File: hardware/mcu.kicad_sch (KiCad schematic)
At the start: 56 parts, among them J10 PRPC001DAAN-RC, J11 PRPC006SAAN-RC, J12 PRPC004SAAN-RC, J8 SBH11-NBPC-D05-SM-BK, J9 PRPC006SAAN-RC, U5 AT25SF081B-SSHD-B, U6 MCP9808T-E/MS, U7 STM32L552CET6, Y1 ABS05-32.768KHZ-9-T, Y2 ECS-160-9-37-CKM-TR3

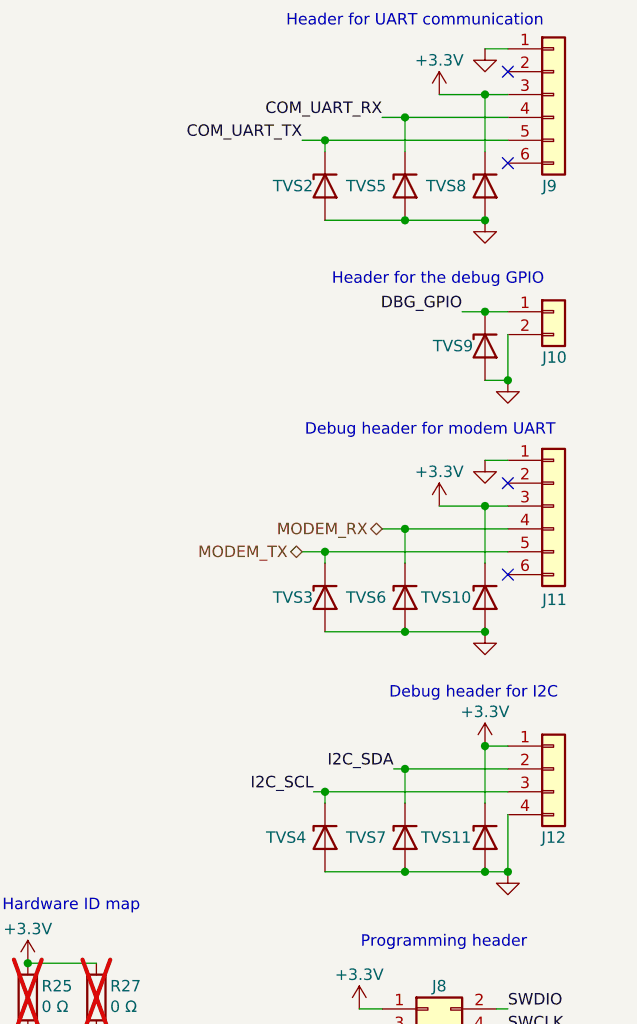
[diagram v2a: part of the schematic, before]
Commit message: HW: Re-layout TVS diodes
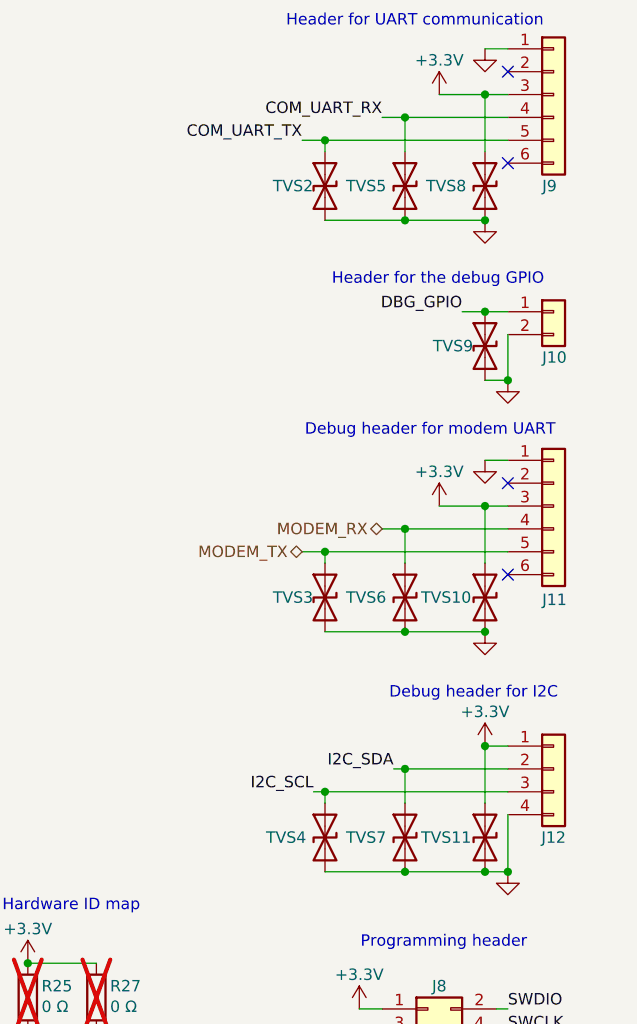
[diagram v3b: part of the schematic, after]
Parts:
- TVS10, TVS11, TVS2, TVS3, TVS4, TVS5, TVS6, TVS7, TVS8, TVS9: value CPDUC5V0USP-HF -> CPDQC5V0ESPC-HF; footprint Diode_SMD:D_0603_1608Metric_Pad1.05x0.95mm_HandSolder -> Diode_SMD:D_0402_1005Metric_Pad0.77x0.64mm_HandSolder; symbol Device:D_Zener -> Device:D_TVS; Digi-Key Part Number 641-1765-1-ND -> 641-1895-1-ND; Manufacturer Part Number CPDUC5V0USP-HF -> CPDQC5V0ESPC-HF
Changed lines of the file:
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@@
 	)
 	(symbol
-		(lib_id "Device:D_Zener")
+		(lib_id "Device:D_TVS")
 		(at 271.78 101.6 90)
 		(mirror x)
@@
 			)
 		)
-		(property "Value" "CPDUC5V0USP-HF"
+		(property "Value" "CPDQC5V0ESPC-HF"
 			(at 261.62 102.87 90)
 			(effects
@@
 			)
 		)
-		(property "Footprint" "Diode_SMD:D_0603_1608Metric_Pad1.05x0.95mm_HandSolder"
+		(property "Footprint" "Diode_SMD:D_0402_1005Metric_Pad0.77x0.64mm_HandSolder"
 			(at 271.78 101.6 0)
 			(effects
@@
 			)
 		)
-		(property "Description" ""
+		(property "Description" "Bidirectional transient-voltage-suppression diode"
 			(at 271.78 101.6 0)
 			(effects
@@
 			)
 		)
-		(property "Digi-Key Part Number" "641-1765-1-ND"
+		(property "Digi-Key Part Number" "641-1895-1-ND"
 			(at 271.78 101.6 0)
 			(effects
@@
 			)
 		)
-		(property "Manufacturer Part Number" "CPDUC5V0USP-HF"
+		(property "Manufacturer Part Number" "CPDQC5V0ESPC-HF"
 			(at 271.78 101.6 0)
 			(effects
@@
 	)
 	(symbol
-		(lib_id "Device:D_Zener")
+		(lib_id "Device:D_TVS")
 		(at 254 101.6 90)
 		(mirror x)
@@
 			)
 		)
-		(property "Value" "CPDUC5V0USP-HF"
+		(property "Value" "CPDQC5V0ESPC-HF"
 			(at 243.84 102.87 90)
 			(effects
@@
 			)
 		)
-		(property "Footprint" "Diode_SMD:D_0603_1608Metric_Pad1.05x0.95mm_HandSolder"
+		(property "Footprint" "Diode_SMD:D_0402_1005Metric_Pad0.77x0.64mm_HandSolder"
 			(at 254 101.6 0)
 			(effects
@@
 			)
 		)
-		(property "Description" ""
+		(property "Description" "Bidirectional transient-voltage-suppression diode"
 			(at 254 101.6 0)
 			(effects
@@
 			)
 		)
-		(property "Digi-Key Part Number" "641-1765-1-ND"
+		(property "Digi-Key Part Number" "641-1895-1-ND"
 			(at 254 101.6 0)
 			(effects
@@
 			)
 		)
-		(property "Manufacturer Part Number" "CPDUC5V0USP-HF"
+		(property "Manufacturer Part Number" "CPDQC5V0ESPC-HF"
 			(at 254 101.6 0)
 			(effects
@@
 	)
 	(symbol
-		(lib_id "Device:D_Zener")
+		(lib_id "Device:D_TVS")
 		(at 271.78 73.66 90)
 		(mirror x)
@@
 			)
 		)
-		(property "Value" "CPDUC5V0USP-HF"
+		(property "Value" "CPDQC5V0ESPC-HF"
 			(at 261.62 74.93 90)
 			(effects
@@
 			)
 		)
-		(property "Footprint" "Diode_SMD:D_0603_1608Metric_Pad1.05x0.95mm_HandSolder"
+		(property "Footprint" "Diode_SMD:D_0402_1005Metric_Pad0.77x0.64mm_HandSolder"
 			(at 271.78 73.66 0)
 			(effects
@@
 			)
 		)
-		(property "Description" ""
+		(property "Description" "Bidirectional transient-voltage-suppression diode"
 			(at 271.78 73.66 0)
 			(effects
@@
 			)
 		)
-		(property "Digi-Key Part Number" "641-1765-1-ND"
+		(property "Digi-Key Part Number" "641-1895-1-ND"
 			(at 271.78 73.66 0)
 			(effects
@@
 			)
 		)
-		(property "Manufacturer Part Number" "CPDUC5V0USP-HF"
+		(property "Manufacturer Part Number" "CPDQC5V0ESPC-HF"
 			(at 271.78 73.66 0)
 			(effects
@@
 	)
 	(symbol
-		(lib_id "Device:D_Zener")
+		(lib_id "Device:D_TVS")
 		(at 262.89 101.6 90)
 		(mirror x)
@@
 			)
 		)
-		(property "Value" "CPDUC5V0USP-HF"
+		(property "Value" "CPDQC5V0ESPC-HF"
 			(at 252.73 102.87 90)
 			(effects
@@
 			)
 		)
-		(property "Footprint" "Diode_SMD:D_0603_1608Metric_Pad1.05x0.95mm_HandSolder"
+		(property "Footprint" "Diode_SMD:D_0402_1005Metric_Pad0.77x0.64mm_HandSolder"
 			(at 262.89 101.6 0)
 			(effects
@@
 			)
 		)
-		(property "Description" ""
+		(property "Description" "Bidirectional transient-voltage-suppression diode"
 			(at 262.89 101.6 0)
 			(effects
@@
 			)
 		)
-		(property "Digi-Key Part Number" "641-1765-1-ND"
+		(property "Digi-Key Part Number" "641-1895-1-ND"
 			(at 262.89 101.6 0)
 			(effects
@@
 			)
 		)
-		(property "Manufacturer Part Number" "CPDUC5V0USP-HF"
+		(property "Manufacturer Part Number" "CPDQC5V0ESPC-HF"
 			(at 262.89 101.6 0)
 			(effects
@@
 	)
 	(symbol
-		(lib_id "Device:D_Zener")
+		(lib_id "Device:D_TVS")
 		(at 262.89 55.88 90)
 		(mirror x)
@@
 			)
 		)
-		(property "Value" "CPDUC5V0USP-HF"
+		(property "Value" "CPDQC5V0ESPC-HF"
 			(at 252.73 57.15 90)
 			(effects
@@
 			)
 		)
-		(property "Footprint" "Diode_SMD:D_0603_1608Metric_Pad1.05x0.95mm_HandSolder"
+		(property "Footprint" "Diode_SMD:D_0402_1005Metric_Pad0.77x0.64mm_HandSolder"
 			(at 262.89 55.88 0)
 			(effects
@@
 			)
 		)
-		(property "Description" ""
+		(property "Description" "Bidirectional transient-voltage-suppression diode"
 			(at 262.89 55.88 0)
 			(effects
@@
 			)
 		)
-		(property "Digi-Key Part Number" "641-1765-1-ND"
+		(property "Digi-Key Part Number" "641-1895-1-ND"
 			(at 262.89 55.88 0)
 			(effects
@@
 			)
 		)
-		(property "Manufacturer Part Number" "CPDUC5V0USP-HF"
+		(property "Manufacturer Part Number" "CPDQC5V0ESPC-HF"
 			(at 262.89 55.88 0)
 			(effects
@@
 	)
 	(symbol
-		(lib_id "Device:D_Zener")
+		(lib_id "Device:D_TVS")
 		(at 271.78 55.88 90)
 		(mirror x)
@@
 			)
 		)
-		(property "Value" "CPDUC5V0USP-HF"
+		(property "Value" "CPDQC5V0ESPC-HF"
 			(at 261.62 57.15 90)
 			(effects
@@
 			)
 		)
-		(property "Footprint" "Diode_SMD:D_0603_1608Metric_Pad1.05x0.95mm_HandSolder"
+		(property "Footprint" "Diode_SMD:D_0402_1005Metric_Pad0.77x0.64mm_HandSolder"
 			(at 271.78 55.88 0)
 			(effects
@@
 			)
 		)
-		(property "Description" ""
+		(property "Description" "Bidirectional transient-voltage-suppression diode"
 			(at 271.78 55.88 0)
 			(effects
@@
 			)
 		)
-		(property "Digi-Key Part Number" "641-1765-1-ND"
+		(property "Digi-Key Part Number" "641-1895-1-ND"
 			(at 271.78 55.88 0)
 			(effects
@@
 			)
 		)
-		(property "Manufacturer Part Number" "CPDUC5V0USP-HF"
+		(property "Manufacturer Part Number" "CPDQC5V0ESPC-HF"
 			(at 271.78 55.88 0)
 			(effects
@@
 	)
 	(symbol
-		(lib_id "Device:D_Zener")
+		(lib_id "Device:D_TVS")
 		(at 254 128.27 90)
 		(mirror x)
@@
 			)
 		)
-		(property "Value" "CPDUC5V0USP-HF"
+		(property "Value" "CPDQC5V0ESPC-HF"
 			(at 243.84 129.54 90)
 			(effects
@@
 			)
 		)
-		(property "Footprint" "Diode_SMD:D_0603_1608Metric_Pad1.05x0.95mm_HandSolder"
+		(property "Footprint" "Diode_SMD:D_0402_1005Metric_Pad0.77x0.64mm_HandSolder"
 			(at 254 128.27 0)
 			(effects
@@
 			)
 		)
-		(property "Description" ""
+		(property "Description" "Bidirectional transient-voltage-suppression diode"
 			(at 254 128.27 0)
 			(effects
@@
 			)
 		)
-		(property "Digi-Key Part Number" "641-1765-1-ND"
+		(property "Digi-Key Part Number" "641-1895-1-ND"
 			(at 254 128.27 0)
 			(effects
@@
 			)
 		)
-		(property "Manufacturer Part Number" "CPDUC5V0USP-HF"
+		(property "Manufacturer Part Number" "CPDQC5V0ESPC-HF"
 			(at 254 128.27 0)
 			(effects
@@
 	)
 	(symbol
-		(lib_id "Device:D_Zener")
+		(lib_id "Device:D_TVS")
 		(at 254 55.88 90)
 		(mirror x)
@@
 			)
 		)
-		(property "Value" "CPDUC5V0USP-HF"
+		(property "Value" "CPDQC5V0ESPC-HF"
 			(at 243.84 57.15 90)
 			(effects
@@
 			)
 		)
-		(property "Footprint" "Diode_SMD:D_0603_1608Metric_Pad1.05x0.95mm_HandSolder"
+		(property "Footprint" "Diode_SMD:D_0402_1005Metric_Pad0.77x0.64mm_HandSolder"
 			(at 254 55.88 0)
 			(effects
@@
 			)
 		)
-		(property "Description" ""
+		(property "Description" "Bidirectional transient-voltage-suppression diode"
 			(at 254 55.88 0)
 			(effects
@@
 			)
 		)
-		(property "Digi-Key Part Number" "641-1765-1-ND"
+		(property "Digi-Key Part Number" "641-1895-1-ND"
 			(at 254 55.88 0)
 			(effects
@@
 			)
 		)
-		(property "Manufacturer Part Number" "CPDUC5V0USP-HF"
+		(property "Manufacturer Part Number" "CPDQC5V0ESPC-HF"
 			(at 254 55.88 0)
 			(effects
@@
 	)
 	(symbol
-		(lib_id "Device:D_Zener")
+		(lib_id "Device:D_TVS")
 		(at 262.89 128.27 90)
 		(mirror x)
@@
 			)
 		)
-		(property "Value" "CPDUC5V0USP-HF"
+		(property "Value" "CPDQC5V0ESPC-HF"
 			(at 252.73 129.54 90)
 			(effects
@@
 			)
 		)
-		(property "Footprint" "Diode_SMD:D_0603_1608Metric_Pad1.05x0.95mm_HandSolder"
+		(property "Footprint" "Diode_SMD:D_0402_1005Metric_Pad0.77x0.64mm_HandSolder"
 			(at 262.89 128.27 0)
 			(effects
@@
 			)
 		)
-		(property "Description" ""
+		(property "Description" "Bidirectional transient-voltage-suppression diode"
 			(at 262.89 128.27 0)
 			(effects
@@
 			)
 		)
-		(property "Digi-Key Part Number" "641-1765-1-ND"
+		(property "Digi-Key Part Number" "641-1895-1-ND"
 			(at 262.89 128.27 0)
 			(effects
@@
 			)
 		)
-		(property "Manufacturer Part Number" "CPDUC5V0USP-HF"
+		(property "Manufacturer Part Number" "CPDQC5V0ESPC-HF"
 			(at 262.89 128.27 0)
 			(effects
@@
 	)
 	(symbol
-		(lib_id "Device:D_Zener")
+		(lib_id "Device:D_TVS")
 		(at 271.78 128.27 90)
 		(mirror x)
@@
 			)
 		)
-		(property "Value" "CPDUC5V0USP-HF"
+		(property "Value" "CPDQC5V0ESPC-HF"
 			(at 261.62 129.54 90)
 			(effects
@@
 			)
 		)
-		(property "Footprint" "Diode_SMD:D_0603_1608Metric_Pad1.05x0.95mm_HandSolder"
+		(property "Footprint" "Diode_SMD:D_0402_1005Metric_Pad0.77x0.64mm_HandSolder"
 			(at 271.78 128.27 0)
 			(effects
@@
 			)
 		)
-		(property "Description" ""
+		(property "Description" "Bidirectional transient-voltage-suppression diode"
 			(at 271.78 128.27 0)
 			(effects
@@
 			)
 		)
-		(property "Digi-Key Part Number" "641-1765-1-ND"
+		(property "Digi-Key Part Number" "641-1895-1-ND"
 			(at 271.78 128.27 0)
 			(effects
@@
 			)
 		)
-		(property "Manufacturer Part Number" "CPDUC5V0USP-HF"
+		(property "Manufacturer Part Number" "CPDQC5V0ESPC-HF"
 			(at 271.78 128.27 0)
 			(effects

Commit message: HW: Replace TVS diode
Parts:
- TVS10, TVS11, TVS2, TVS3, TVS4, TVS5, TVS6, TVS7, TVS8, TVS9: value CPDQC5V0ESPC-HF -> D5V0F1B2WS-7; footprint Diode_SMD:D_0402_1005Metric_Pad0.77x0.64mm_HandSolder -> Diode_SMD:D_SOD-323_HandSoldering; Digi-Key Part Number 641-1895-1-ND -> 31-D5V0F1B2WS-7CT-ND; Manufacturer Comchip Technology -> Diodes Incorporated; Manufacturer Part Number CPDQC5V0ESPC-HF -> D5V0F1B2WS-7
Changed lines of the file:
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@@
 			)
 		)
-		(property "Value" "CPDQC5V0ESPC-HF"
+		(property "Value" "D5V0F1B2WS-7"
 			(at 261.62 102.87 90)
 			(effects
@@
 			)
 		)
-		(property "Footprint" "Diode_SMD:D_0402_1005Metric_Pad0.77x0.64mm_HandSolder"
+		(property "Footprint" "Diode_SMD:D_SOD-323_HandSoldering"
 			(at 271.78 101.6 0)
 			(effects
@@
 			)
 		)
-		(property "Digi-Key Part Number" "641-1895-1-ND"
+		(property "Digi-Key Part Number" "31-D5V0F1B2WS-7CT-ND"
 			(at 271.78 101.6 0)
 			(effects
@@
 			)
 		)
-		(property "Manufacturer" "Comchip Technology"
+		(property "Manufacturer" "Diodes Incorporated"
 			(at 271.78 101.6 0)
 			(effects
@@
 			)
 		)
-		(property "Manufacturer Part Number" "CPDQC5V0ESPC-HF"
+		(property "Manufacturer Part Number" "D5V0F1B2WS-7"
 			(at 271.78 101.6 0)
 			(effects
@@
 			)
 		)
-		(property "Value" "CPDQC5V0ESPC-HF"
+		(property "Value" "D5V0F1B2WS-7"
 			(at 243.84 102.87 90)
 			(effects
@@
 			)
 		)
-		(property "Footprint" "Diode_SMD:D_0402_1005Metric_Pad0.77x0.64mm_HandSolder"
+		(property "Footprint" "Diode_SMD:D_SOD-323_HandSoldering"
 			(at 254 101.6 0)
 			(effects
@@
 			)
 		)
-		(property "Digi-Key Part Number" "641-1895-1-ND"
+		(property "Digi-Key Part Number" "31-D5V0F1B2WS-7CT-ND"
 			(at 254 101.6 0)
 			(effects
@@
 			)
 		)
-		(property "Manufacturer" "Comchip Technology"
+		(property "Manufacturer" "Diodes Incorporated"
 			(at 254 101.6 0)
 			(effects
@@
 			)
 		)
-		(property "Manufacturer Part Number" "CPDQC5V0ESPC-HF"
+		(property "Manufacturer Part Number" "D5V0F1B2WS-7"
 			(at 254 101.6 0)
 			(effects
@@
 			)
 		)
-		(property "Value" "CPDQC5V0ESPC-HF"
+		(property "Value" "D5V0F1B2WS-7"
 			(at 261.62 74.93 90)
 			(effects
@@
 			)
 		)
-		(property "Footprint" "Diode_SMD:D_0402_1005Metric_Pad0.77x0.64mm_HandSolder"
+		(property "Footprint" "Diode_SMD:D_SOD-323_HandSoldering"
 			(at 271.78 73.66 0)
 			(effects
@@
 			)
 		)
-		(property "Digi-Key Part Number" "641-1895-1-ND"
+		(property "Digi-Key Part Number" "31-D5V0F1B2WS-7CT-ND"
 			(at 271.78 73.66 0)
 			(effects
@@
 			)
 		)
-		(property "Manufacturer" "Comchip Technology"
+		(property "Manufacturer" "Diodes Incorporated"
 			(at 271.78 73.66 0)
 			(effects
@@
 			)
 		)
-		(property "Manufacturer Part Number" "CPDQC5V0ESPC-HF"
+		(property "Manufacturer Part Number" "D5V0F1B2WS-7"
 			(at 271.78 73.66 0)
 			(effects
@@
 			)
 		)
-		(property "Value" "CPDQC5V0ESPC-HF"
+		(property "Value" "D5V0F1B2WS-7"
 			(at 252.73 102.87 90)
 			(effects
@@
 			)
 		)
-		(property "Footprint" "Diode_SMD:D_0402_1005Metric_Pad0.77x0.64mm_HandSolder"
+		(property "Footprint" "Diode_SMD:D_SOD-323_HandSoldering"
 			(at 262.89 101.6 0)
 			(effects
@@
 			)
 		)
-		(property "Digi-Key Part Number" "641-1895-1-ND"
+		(property "Digi-Key Part Number" "31-D5V0F1B2WS-7CT-ND"
 			(at 262.89 101.6 0)
 			(effects
@@
 			)
 		)
-		(property "Manufacturer" "Comchip Technology"
+		(property "Manufacturer" "Diodes Incorporated"
 			(at 262.89 101.6 0)
 			(effects
@@
 			)
 		)
-		(property "Manufacturer Part Number" "CPDQC5V0ESPC-HF"
+		(property "Manufacturer Part Number" "D5V0F1B2WS-7"
 			(at 262.89 101.6 0)
 			(effects
@@
 			)
 		)
-		(property "Value" "CPDQC5V0ESPC-HF"
+		(property "Value" "D5V0F1B2WS-7"
 			(at 252.73 57.15 90)
 			(effects
@@
 			)
 		)
-		(property "Footprint" "Diode_SMD:D_0402_1005Metric_Pad0.77x0.64mm_HandSolder"
+		(property "Footprint" "Diode_SMD:D_SOD-323_HandSoldering"
 			(at 262.89 55.88 0)
 			(effects
@@
 			)
 		)
-		(property "Digi-Key Part Number" "641-1895-1-ND"
+		(property "Digi-Key Part Number" "31-D5V0F1B2WS-7CT-ND"
 			(at 262.89 55.88 0)
 			(effects
@@
 			)
 		)
-		(property "Manufacturer" "Comchip Technology"
+		(property "Manufacturer" "Diodes Incorporated"
 			(at 262.89 55.88 0)
 			(effects
@@
 			)
 		)
-		(property "Manufacturer Part Number" "CPDQC5V0ESPC-HF"
+		(property "Manufacturer Part Number" "D5V0F1B2WS-7"
 			(at 262.89 55.88 0)
 			(effects
@@
 			)
 		)
-		(property "Value" "CPDQC5V0ESPC-HF"
+		(property "Value" "D5V0F1B2WS-7"
 			(at 261.62 57.15 90)
 			(effects
@@
 			)
 		)
-		(property "Footprint" "Diode_SMD:D_0402_1005Metric_Pad0.77x0.64mm_HandSolder"
+		(property "Footprint" "Diode_SMD:D_SOD-323_HandSoldering"
 			(at 271.78 55.88 0)
 			(effects
@@
 			)
 		)
-		(property "Digi-Key Part Number" "641-1895-1-ND"
+		(property "Digi-Key Part Number" "31-D5V0F1B2WS-7CT-ND"
 			(at 271.78 55.88 0)
 			(effects
@@
 			)
 		)
-		(property "Manufacturer" "Comchip Technology"
+		(property "Manufacturer" "Diodes Incorporated"
 			(at 271.78 55.88 0)
 			(effects
@@
 			)
 		)
-		(property "Manufacturer Part Number" "CPDQC5V0ESPC-HF"
+		(property "Manufacturer Part Number" "D5V0F1B2WS-7"
 			(at 271.78 55.88 0)
 			(effects
@@
 			)
 		)
-		(property "Value" "CPDQC5V0ESPC-HF"
+		(property "Value" "D5V0F1B2WS-7"
 			(at 243.84 129.54 90)
 			(effects
@@
 			)
 		)
-		(property "Footprint" "Diode_SMD:D_0402_1005Metric_Pad0.77x0.64mm_HandSolder"
+		(property "Footprint" "Diode_SMD:D_SOD-323_HandSoldering"
 			(at 254 128.27 0)
 			(effects
@@
 			)
 		)
-		(property "Digi-Key Part Number" "641-1895-1-ND"
+		(property "Digi-Key Part Number" "31-D5V0F1B2WS-7CT-ND"
 			(at 254 128.27 0)
 			(effects
@@
 			)
 		)
-		(property "Manufacturer" "Comchip Technology"
+		(property "Manufacturer" "Diodes Incorporated"
 			(at 254 128.27 0)
 			(effects
@@
 			)
 		)
-		(property "Manufacturer Part Number" "CPDQC5V0ESPC-HF"
+		(property "Manufacturer Part Number" "D5V0F1B2WS-7"
 			(at 254 128.27 0)
 			(effects
@@
 			)
 		)
-		(property "Value" "CPDQC5V0ESPC-HF"
+		(property "Value" "D5V0F1B2WS-7"
 			(at 243.84 57.15 90)
 			(effects
@@
 			)
 		)
-		(property "Footprint" "Diode_SMD:D_0402_1005Metric_Pad0.77x0.64mm_HandSolder"
+		(property "Footprint" "Diode_SMD:D_SOD-323_HandSoldering"
 			(at 254 55.88 0)
 			(effects
@@
 			)
 		)
-		(property "Digi-Key Part Number" "641-1895-1-ND"
+		(property "Digi-Key Part Number" "31-D5V0F1B2WS-7CT-ND"
 			(at 254 55.88 0)
 			(effects
@@
 			)
 		)
-		(property "Manufacturer" "Comchip Technology"
+		(property "Manufacturer" "Diodes Incorporated"
 			(at 254 55.88 0)
 			(effects
@@
 			)
 		)
-		(property "Manufacturer Part Number" "CPDQC5V0ESPC-HF"
+		(property "Manufacturer Part Number" "D5V0F1B2WS-7"
 			(at 254 55.88 0)
 			(effects
@@
 			)
 		)
-		(property "Value" "CPDQC5V0ESPC-HF"
+		(property "Value" "D5V0F1B2WS-7"
 			(at 252.73 129.54 90)
 			(effects
@@
 			)
 		)
-		(property "Footprint" "Diode_SMD:D_0402_1005Metric_Pad0.77x0.64mm_HandSolder"
+		(property "Footprint" "Diode_SMD:D_SOD-323_HandSoldering"
 			(at 262.89 128.27 0)
 			(effects
@@
 			)
 		)
-		(property "Digi-Key Part Number" "641-1895-1-ND"
+		(property "Digi-Key Part Number" "31-D5V0F1B2WS-7CT-ND"
 			(at 262.89 128.27 0)
 			(effects
@@
 			)
 		)
-		(property "Manufacturer" "Comchip Technology"
+		(property "Manufacturer" "Diodes Incorporated"
 			(at 262.89 128.27 0)
 			(effects
@@
 			)
 		)
-		(property "Manufacturer Part Number" "CPDQC5V0ESPC-HF"
+		(property "Manufacturer Part Number" "D5V0F1B2WS-7"
 			(at 262.89 128.27 0)
 			(effects
@@
 			)
 		)
-		(property "Value" "CPDQC5V0ESPC-HF"
+		(property "Value" "D5V0F1B2WS-7"
 			(at 261.62 129.54 90)
 			(effects
@@
 			)
 		)
-		(property "Footprint" "Diode_SMD:D_0402_1005Metric_Pad0.77x0.64mm_HandSolder"
+		(property "Footprint" "Diode_SMD:D_SOD-323_HandSoldering"
 			(at 271.78 128.27 0)
 			(effects
@@
 			)
 		)
-		(property "Digi-Key Part Number" "641-1895-1-ND"
+		(property "Digi-Key Part Number" "31-D5V0F1B2WS-7CT-ND"
 			(at 271.78 128.27 0)
 			(effects
@@
 			)
 		)
-		(property "Manufacturer" "Comchip Technology"
+		(property "Manufacturer" "Diodes Incorporated"
 			(at 271.78 128.27 0)
 			(effects
@@
 			)
 		)
-		(property "Manufacturer Part Number" "CPDQC5V0ESPC-HF"
+		(property "Manufacturer Part Number" "D5V0F1B2WS-7"
 			(at 271.78 128.27 0)
 			(effects
